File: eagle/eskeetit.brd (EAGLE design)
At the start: 47 x 28 mm, 46 parts, among them M1 WIRELESS-NRF24L01, U1 GY-521MPU6050, U2 TPS63000DRCR, Y1 20MHz

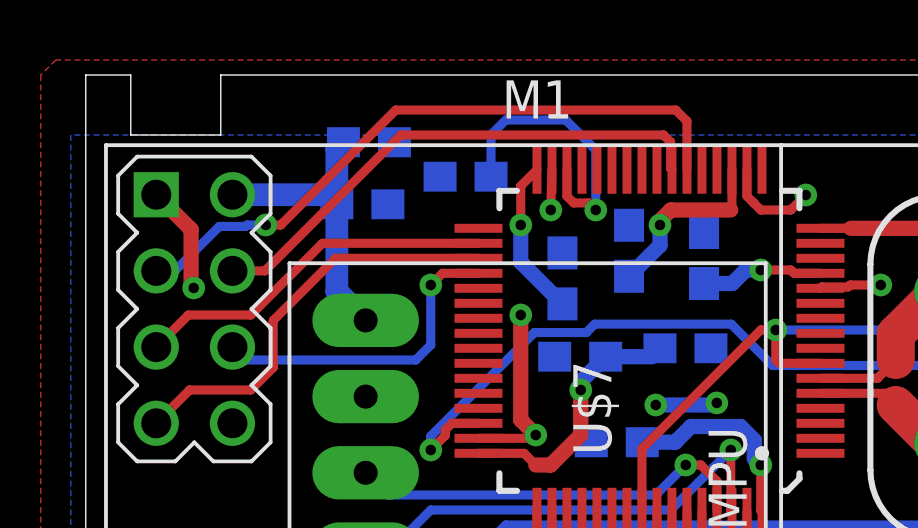
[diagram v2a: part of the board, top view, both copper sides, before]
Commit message: fixed some bottlenecks
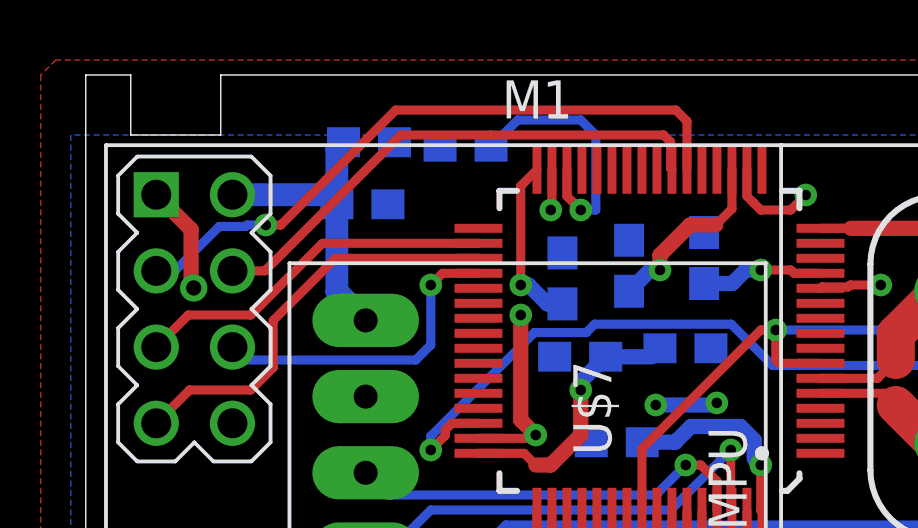
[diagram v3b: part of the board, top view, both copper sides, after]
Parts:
- moved C14 1.00 mm to (12.7, 25.6)
- moved C23 0.50 mm to (18.1, 21.6)
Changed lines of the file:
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@@
 <attribute name="SPICEPREFIX" value="C" x="-5" y="-31" size="1.778" layer="27" rot="R270" display="off"/>
 </element>
-<element name="C14" library="capstone" package="RCL_C0603" value="4.7uF" x="12.66" y="24.61" smashed="yes" rot="MR0">
-<attribute name="NAME" x="13.295" y="25.245" size="1.27" layer="26" rot="MR0"/>
-<attribute name="SPICEPREFIX" value="C" x="-40.68" y="-30" size="1.778" layer="28" rot="MR0" display="off"/>
-<attribute name="VALUE" x="13.295" y="22.705" size="1.27" layer="28" rot="MR0"/>
+<element name="C14" library="capstone" package="RCL_C0603" value="4.7uF" x="12.66" y="25.61" smashed="yes" rot="MR0">
+<attribute name="NAME" x="13.295" y="26.245" size="1.27" layer="26" rot="MR0"/>
+<attribute name="SPICEPREFIX" value="C" x="-40.68" y="-29" size="1.778" layer="28" rot="MR0" display="off"/>
+<attribute name="VALUE" x="13.295" y="23.705" size="1.27" layer="28" rot="MR0"/>
 </element>
 <element name="C15" library="capstone" package="RCL_C0603" value="4.7uF" x="37.31" y="6.11" smashed="yes">
@@
 <attribute name="VALUE" x="17.115" y="16.705" size="1.27" layer="28" rot="MR0"/>
 </element>
-<element name="C23" library="capstone" package="RCL_C0603" value="100nF" x="18.11" y="22.14" smashed="yes" rot="MR90">
-<attribute name="NAME" x="18.245" y="21.505" size="1.27" layer="26" rot="MR90"/>
-<attribute name="SPICEPREFIX" value="C" x="-36.5" y="62.78" size="1.778" layer="28" rot="MR90" display="off"/>
-<attribute name="VALUE" x="16.205" y="21.505" size="1.27" layer="28" rot="MR90"/>
+<element name="C23" library="capstone" package="RCL_C0603" value="100nF" x="18.11" y="21.64" smashed="yes" rot="MR90">
+<attribute name="NAME" x="18.245" y="21.005" size="1.27" layer="26" rot="MR90"/>
+<attribute name="SPICEPREFIX" value="C" x="-36.5" y="62.28" size="1.778" layer="28" rot="MR90" display="off"/>
+<attribute name="VALUE" x="16.205" y="21.005" size="1.27" layer="28" rot="MR90"/>
 </element>
 <element name="C3" library="capstone" package="RCL_C0603" value="4.7uF" x="19.99" y="18.89" smashed="yes" rot="MR180">
@@
 <via x="26.5" y="21" extent="1-16" drill="0.35"/>
 <wire x1="20.76375" y1="12.3352" x2="22" y2="12.3352" width="0.3048" layer="1"/>
-<wire x1="15.54" y1="24.84" x2="15.5" y2="23.5" width="0.3048" layer="1"/>
+<wire x1="15.5" y1="23.5" x2="15.54" y2="23.50119375" width="0.3048" layer="1"/>
+<wire x1="15.54" y1="24.84" x2="15.54" y2="23.50119375" width="0.3048" layer="1"/>
 <via x="15.5" y="23.5" extent="1-16" drill="0.35"/>
 <wire x1="20.54" y1="13.44" x2="20.54" y2="12.55895" width="0.3048" layer="1"/>
@@
 <wire x1="3.5104" y1="21" x2="3.59835" y2="20.91205" width="0.508" layer="1"/>
 <wire x1="3.59835" y1="20.91205" x2="3.59835" y2="20.90165" width="0.508" layer="1"/>
-<via x="3.59835" y="20.90165" extent="1-16" drill="0.35"/>
+<via x="3.59835" y="20.90165" extent="1-16" drill="0.508"/>
 <wire x1="40.13" y1="3.2" x2="40.13" y2="2.13" width="1.27" layer="16"/>
 <wire x1="40.13" y1="2.13" x2="39.651" y2="1.651" width="1.27" layer="16"/>
@@
 <wire x1="22.5" y1="21.5" x2="23.49895" y2="21.5" width="0.3048" layer="1"/>
 <wire x1="21.54" y1="24.84" x2="21.54" y2="23.54" width="0.3048" layer="1"/>
-<wire x1="21.54" y1="23.54" x2="21.5" y2="23.5" width="0.3048" layer="1"/>
-<wire x1="21.5" y1="23.5" x2="19.5" y2="23.5" width="0.508" layer="1"/>
-<wire x1="19.5" y1="23.5" x2="19.1406" y2="23.1406" width="0.508" layer="1"/>
-<wire x1="19.1406" y1="23.1406" x2="19.1406" y2="23" width="0.508" layer="1"/>
-<via x="19.1406" y="23" extent="1-16" drill="0.35"/>
-<wire x1="19.1406" y1="23" x2="19.1406" y2="22.3206" width="0.508" layer="16"/>
-<wire x1="19.1406" y1="22.3206" x2="18.11" y2="21.29" width="0.508" layer="16"/>
-<wire x1="15.89" y1="20.37" x2="14.5" y2="21.76" width="0.508" layer="16"/>
-<wire x1="14.5" y1="21.76" x2="14.5" y2="23" width="0.508" layer="16"/>
-<via x="14.5" y="23" extent="1-16" drill="0.35"/>
-<wire x1="14.5" y1="23" x2="14.5" y2="24.3" width="0.3048" layer="1"/>
-<wire x1="14.5" y1="24.3" x2="15.04" y2="24.84" width="0.3048" layer="1"/>
+<wire x1="21.54" y1="23.54" x2="21" y2="23" width="0.3048" layer="1"/>
+<wire x1="21" y1="23" x2="20.1406" y2="23" width="0.508" layer="1"/>
+<wire x1="20.1406" y1="23" x2="19.1406" y2="22" width="0.508" layer="1"/>
+<wire x1="19.1406" y1="22" x2="19.1406" y2="21.5" width="0.508" layer="1"/>
+<via x="19.1406" y="21.5" extent="1-16" drill="0.35"/>
+<wire x1="19.1406" y1="21.5" x2="18.82" y2="21.5" width="0.508" layer="16"/>
+<wire x1="18.82" y1="21.5" x2="18.11" y2="20.79" width="0.508" layer="16"/>
+<wire x1="15.89" y1="20.37" x2="15.39" y2="20.37" width="0.508" layer="16"/>
+<wire x1="15.39" y1="20.37" x2="14.76" y2="21" width="0.508" layer="16"/>
+<wire x1="14.5" y1="21" x2="14.76" y2="21" width="0.508" layer="16"/>
+<via x="14.5" y="21" extent="1-16" drill="0.35"/>
+<wire x1="14.5" y1="24.3" x2="14.5" y2="21" width="0.3048" layer="1"/>
+<wire x1="15.04" y1="24.84" x2="14.5" y2="24.3" width="0.3048" layer="1"/>
 <wire x1="18.55" y1="15.76" x2="19.65040625" y2="15.76" width="0.508" layer="16"/>
 <wire x1="19.65040625" y1="15.76" x2="20.17500625" y2="16.2846" width="0.508" layer="16"/>
@@
 <contactref element="U$7" pad="30"/>
 <contactref element="C14" pad="1"/>
-<wire x1="13.51" y1="24.61" x2="13.51" y2="25.99" width="0.3048" layer="16"/>
+<wire x1="13.51" y1="25.61" x2="13.51" y2="25.99" width="0.3048" layer="16"/>
 <wire x1="13.51" y1="25.99" x2="13.5" y2="26" width="0.3048" layer="16"/>
-<wire x1="13.5" y1="26" x2="14" y2="26.5" width="0.3048" layer="16"/>
-<wire x1="14" y1="26.5" x2="16" y2="26.5" width="0.3048" layer="16"/>
-<wire x1="17" y1="25.5" x2="17" y2="23.5" width="0.3048" layer="16"/>
-<via x="17" y="23.5" extent="1-16" drill="0.35"/>
-<wire x1="17" y1="23.5" x2="16.7648" y2="23.7352" width="0.3048" layer="1"/>
-<wire x1="16.7648" y1="23.7352" x2="16.26375" y2="23.7352" width="0.3048" layer="1"/>
+<wire x1="13.51" y1="25.61" x2="13.61" y2="25.61" width="0.3048" layer="16"/>
+<wire x1="13.51" y1="25.61" x2="14.4" y2="26.5" width="0.3048" layer="16"/>
+<wire x1="14.4" y1="26.5" x2="16.5" y2="26.5" width="0.3048" layer="16"/>
+<wire x1="16.5" y1="26.5" x2="17" y2="26" width="0.3048" layer="16"/>
+<wire x1="17" y1="26" x2="17" y2="23.5" width="0.3048" layer="16"/>
+<wire x1="17" y1="23.5" x2="16.5" y2="23.5" width="0.3048" layer="16"/>
+<via x="16.5" y="23.5" extent="1-16" drill="0.35"/>
+<wire x1="16.5" y1="23.5" x2="16.2648" y2="23.7352" width="0.3048" layer="1"/>
+<wire x1="16.2648" y1="23.7352" x2="16.26375" y2="23.7352" width="0.3048" layer="1"/>
 <wire x1="16.26375" y1="23.7352" x2="16.04" y2="23.95895" width="0.3048" layer="1"/>
 <wire x1="16.04" y1="23.95895" x2="16.04" y2="24.84" width="0.3048" layer="1"/>
-<wire x1="16" y1="26.5" x2="17" y2="25.5" width="0.3048" layer="16"/>
 </signal>
 <signal name="MOTOR3">

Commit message: more bottleneck fixes
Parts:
- moved C1 2.55 mm to (6.94, 26.3)
- moved C2 2.06 mm to (7.22, 24.2)
- moved C15 2.00 mm to (39.3, 6.11)
- moved R5 1.61 mm to (42.2, 5.83), turned to 90 degrees
- moved C14 1.12 mm to (12.2, 24.6), flipped to the top, turned to 180 degrees
- moved M1 1.12 mm to (14.6, 16.7)
- moved R7 0.71 mm to (44.7, 7.25)
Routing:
- net GND: track 46.3 -> 41.1 mm
- net 3.3V: track 51.8 -> 46.8 mm
- net N$4: track 9.09 -> 4.56 mm, vias 1 -> 0
- net PWR: track 8.89 -> 13.3 mm
- net SPI2_CE: track 21.7 -> 24.2 mm, vias 1 -> 2
- net SPI2_CS: track 17.5 -> 19.3 mm
- net SPI2_MISO: track 13.9 -> 15.4 mm, vias 0 -> 1
- net PA5: track 36.1 -> 37.5 mm
- net SPI2_SCK: track 12.2 -> 13.0 mm, vias 0 -> 1
- net SPI2_MOSI: track 10.7 -> 11.3 mm

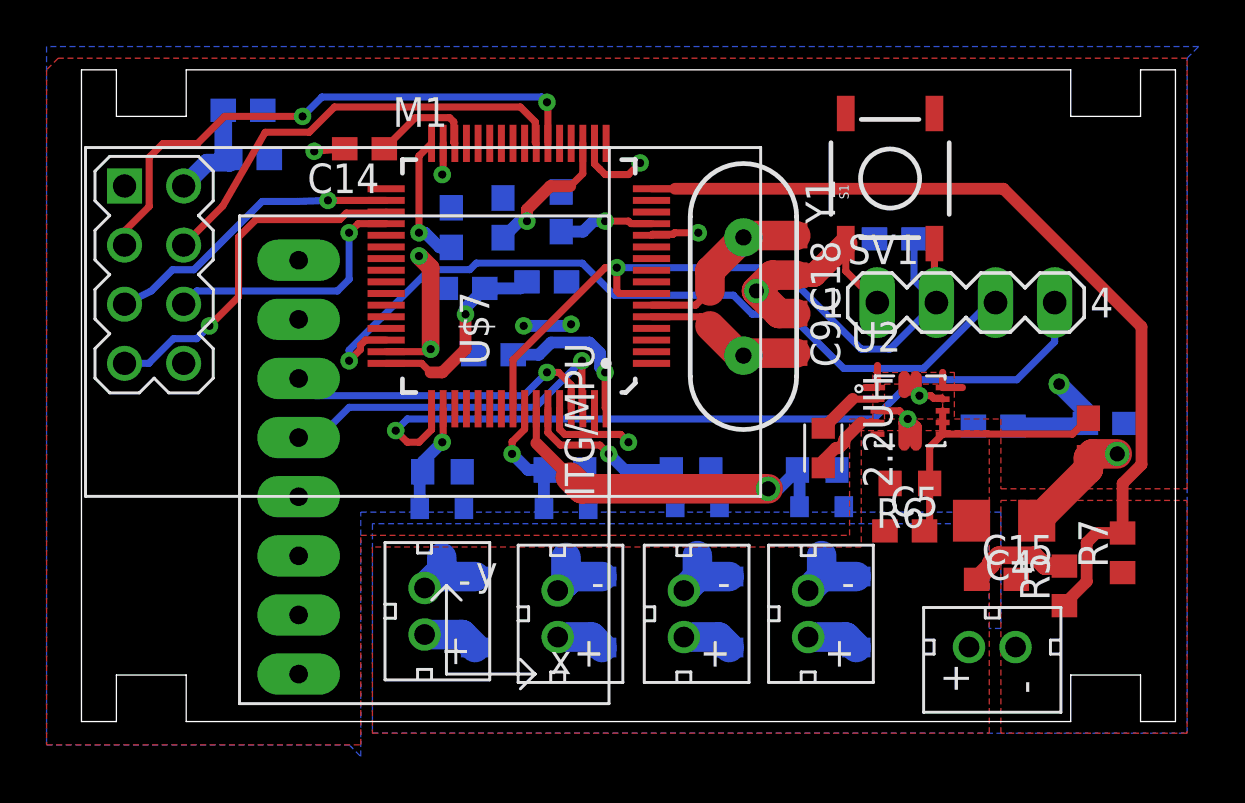
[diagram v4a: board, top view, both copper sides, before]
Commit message: leads are roasting us and we are trying to fix
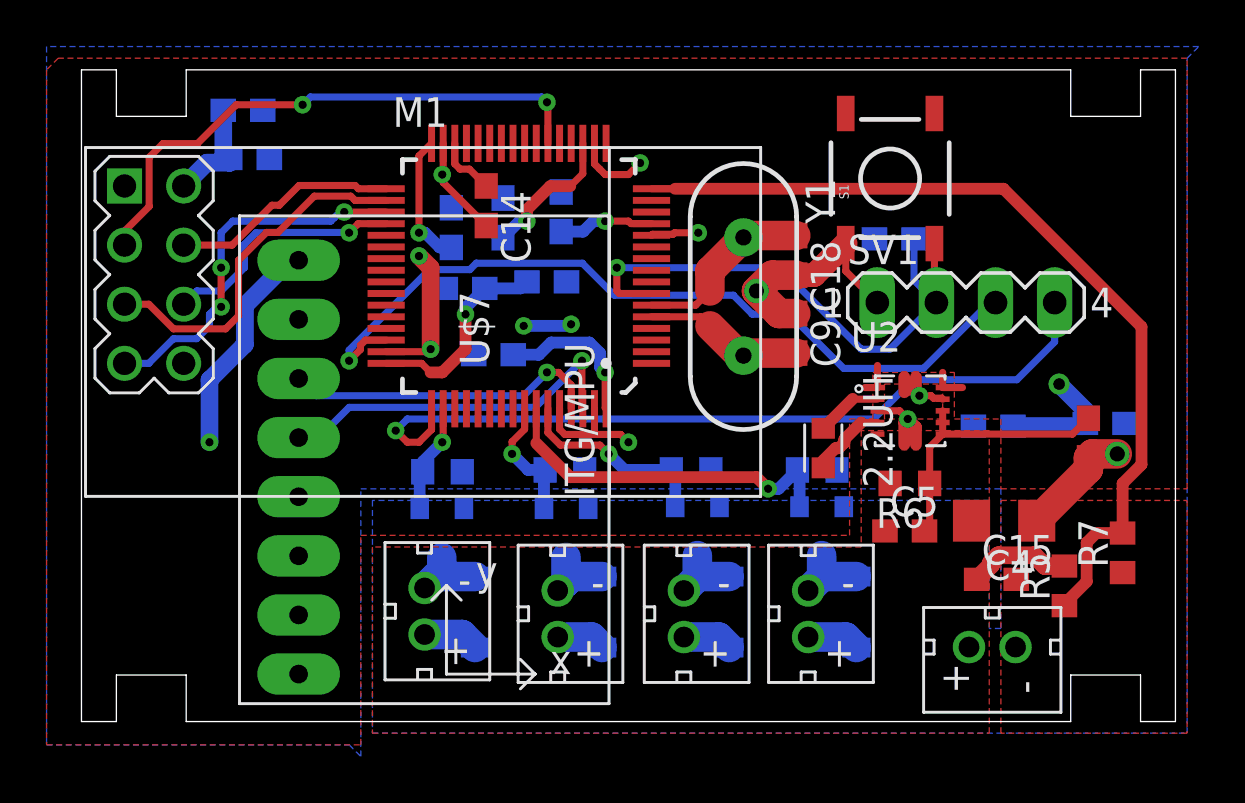
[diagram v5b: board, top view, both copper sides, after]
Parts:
- moved C14 5.78 mm to (17.4, 22.2), turned to 270 degrees
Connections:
- net SPI2_CS: now also U$7.33; no longer U$7.23
- net SWDRST: no longer U$7.56
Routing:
- net 3.3V: track 46.8 -> 56.4 mm, vias 8 -> 9
- net SPI2_CS: track 19.3 -> 9.82 mm
- net SWDRST: track 32.5 -> 24.3 mm
- net SPI2_SCK: track 13.0 -> 15.5 mm, vias 1 -> 0
- net N$4: track 4.56 -> 2.62 mm
- net GND: track 41.1 -> 42.7 mm, vias 11 -> 10
- net SPI2_MISO: track 15.4 -> 16.1 mm, vias 1 -> 3
- net SPI2_MOSI: track 11.3 -> 10.7 mm

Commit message: final revision god I hope this board works
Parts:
- moved C2 2.50 mm to (7.22, 26.7)
- moved C1 2.06 mm to (7.44, 24.3)
- moved R7 1.58 mm to (45.2, 8.75), turned to 180 degrees
- moved R5 1.00 mm to (43.2, 5.83), turned to 180 degrees
- moved U1 0.50 mm to (18.2, 10.4)
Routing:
- net SWDIO: track 34.9 -> 32.0 mm
- net PA5: track 37.5 -> 35.2 mm
- net 3.3V: track 56.4 -> 57.2 mm
